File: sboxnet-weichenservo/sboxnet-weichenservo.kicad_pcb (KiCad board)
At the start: 2 copper layers, 35 parts, among them J1 Screw_Terminal_01x02, J10 Conn_01x03_Male, J11 Conn_01x03_Male, J12 Conn_01x03_Male, J2 Screw_Terminal_01x04, J3 Conn_02x17_Odd_Even, J4 Screw_Terminal_01x04, J5 Conn_01x03_Male, J6 Conn_01x03_Male, J7 Conn_01x03_Male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

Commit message: mit weichen-servo-ctrl
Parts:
- added BAR2: HDSP-4830_2 10x LED, Display:HDSP-4830, F.Cu at (-38.4, 102.3)
- added D3: BAT 54J NXP, Diode_SMD:D_SOD-323F, F.Cu at (-19.5, 146.1)
- added J13: Conn_02x08_Top_Bottom, Connector_PinSocket_2.54mm:PinSocket_2x10_P2.54mm_Vertical, F.Cu at (53.9, 170.0)
- added R2: 100, Resistor_SMD:R_1206_3216Metric_Pad1.42x1.75mm_HandSolder, F.Cu at (-30.5, 152.9)
- added RN1: 4816P-T02-471LF 15x470, Package_SO:SOIC-16W_5.3x10.2mm_P1.27mm, F.Cu at (-15.5, 138.7)
- added RN2: 4816P-2-103 13x 10k, Package_SO:SOIC-14W_7.5x9mm_P1.27mm, F.Cu at (-27.1, 138.0)
- added RN4: 4816P-T02-471LF 15x470, Package_SO:SOIC-16W_5.3x10.2mm_P1.27mm, F.Cu at (-23.7, 106.0)
- added SW5: SW_Push, sboxnet:JTP-1130, F.Cu at (-13.8, 103.8)
- added SW6: SW_Push, sboxnet:JTP-1130, F.Cu at (-24.0, 115.7)
- added SW7: SW_Push, sboxnet:JTP-1130, F.Cu at (-13.8, 111.3)
- added SW8: SW_Push, sboxnet:JTP-1130, F.Cu at (-4.34, 103.8)
- BAR1: value HDSP-4830_2 -> HDSP-4830_2 10x LED
- D1: moved to B.Cu
- RN3: value 8x 100 -> 4816P-1-101 8x 100
- U1: value MIC29302WU -> uA7805 D2PAK; footprint Package_TO_SOT_SMD:TO-263-5_TabPin3 -> Package_TO_SOT_SMD:ATPAK-2; moved to B.Cu
- moved U1 134.5 mm to (70.6, 188.7)
- moved D1 132.9 mm to (56.2, 189.5), turned to 180 degrees
- moved J6 114.7 mm to (70.2, 170.2), turned to 90 degrees
- moved J11 114.6 mm to (70.3, 145.3), turned to 90 degrees
- moved J8 107.5 mm to (70.1, 160.5), turned to 90 degrees
- moved J10 104.2 mm to (70.3, 149.9), turned to 90 degrees
- moved J9 98.2 mm to (70.2, 155.5), turned to 90 degrees
- moved J5 87.3 mm to (70.1, 174.8), turned to 90 degrees
- moved J7 87.3 mm to (70.0, 165.4), turned to 90 degrees
- moved J12 79.9 mm to (70.8, 141.0), turned to 90 degrees
- moved J4 56.6 mm to (133.8, 139.6)
- moved BAR1 49.4 mm to (58.0, 147.0), turned to 270 degrees
- moved J3 47.5 mm to (19.6, 193.2)
- moved J2 36.0 mm to (118.9, 141.6)
- moved J1 12.3 mm to (42.0, 189.5)
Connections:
- U1 pad 2: Net-(C1-Pad1) -> GND
- U1 pad 3: GND -> +5V
- U3 pad 16: VCC -> +5V
- U3 pad 5: Net-(R2-Pad1) -> Net-(D3-Pad1)

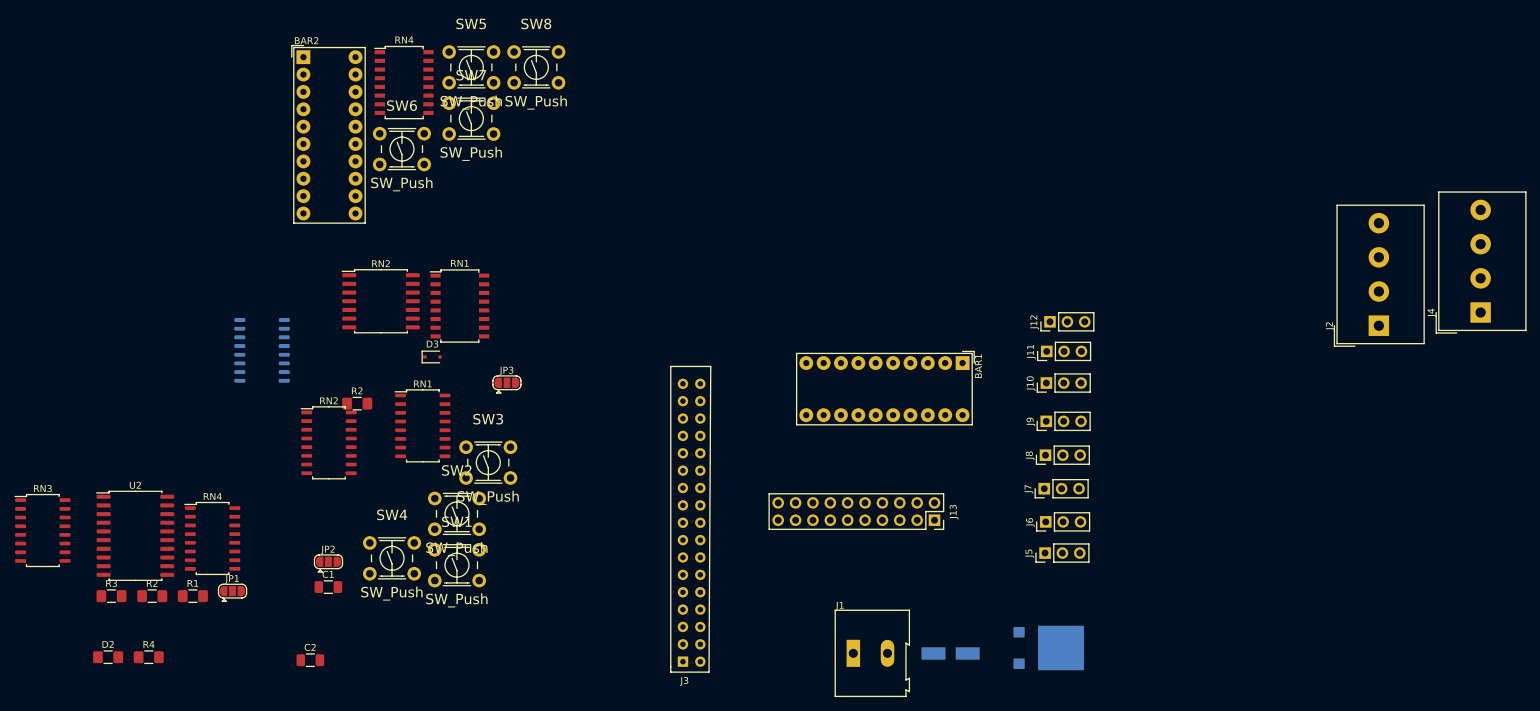
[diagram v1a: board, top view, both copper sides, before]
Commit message: weichenservo mit Modulkennung
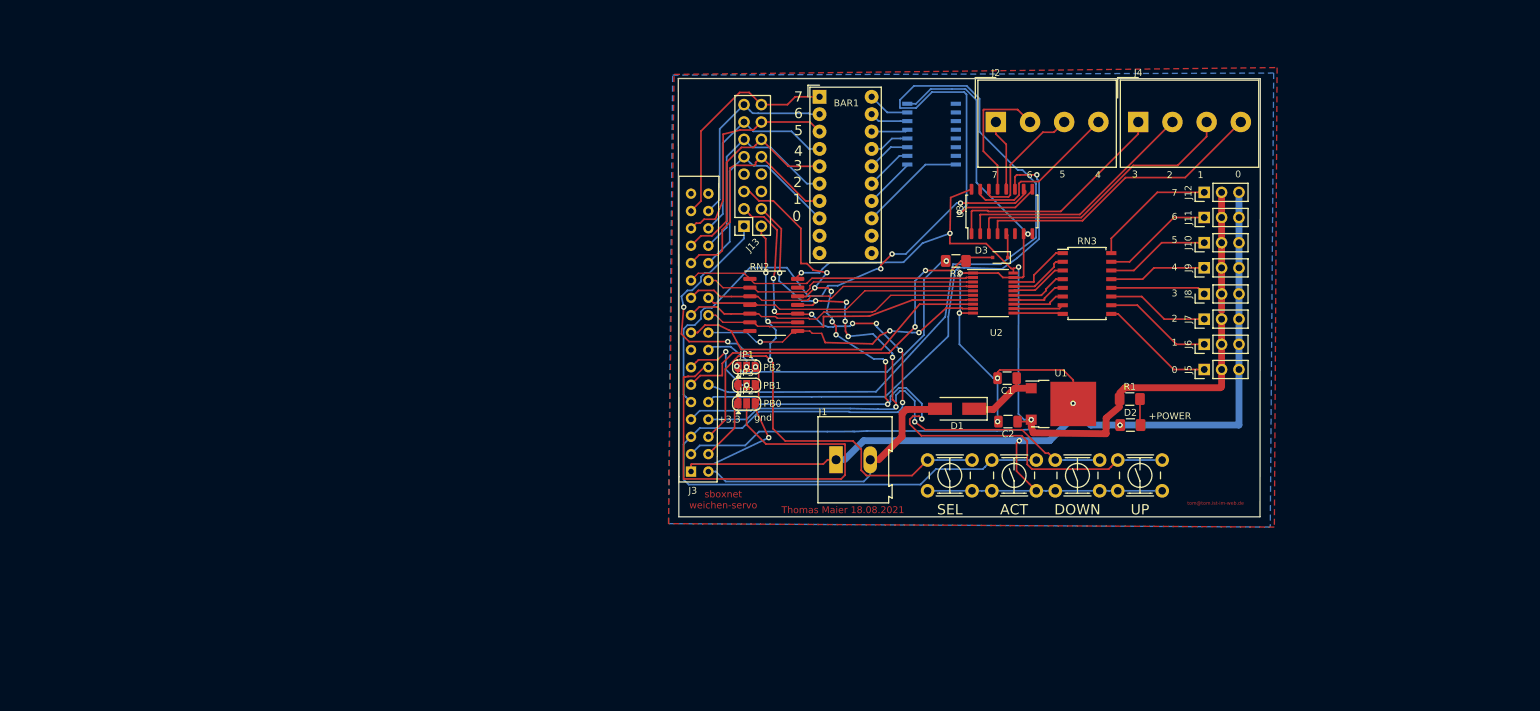
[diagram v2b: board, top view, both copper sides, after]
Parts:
- removed BAR2: HDSP-4830_2 10x LED, Display:HDSP-4830
- removed the R2 at (-30.5, 152.9)
- removed the R2 at (-60.5, 181.1)
- removed R3: 3k, Resistor_SMD:R_1206_3216Metric_Pad1.42x1.75mm_HandSolder
- removed R4: 10k, Resistor_SMD:R_1206_3216Metric_Pad1.42x1.75mm_HandSolder
- removed the RN1 at (-15.5, 138.7)
- removed the RN1 at (-20.9, 156.2)
- removed the RN2 at (-27.1, 138.0)
- removed the RN2 at (-34.7, 158.7)
- removed RN4: 4816P-T02-471LF 15x470, Package_SO:SOIC-16W_5.3x10.2mm_P1.27mm
- removed RN4: R_Network04 10k, Package_SO:SOIC-16_4.55x10.3mm_P1.27mm
- removed SW5, SW6, SW7, SW8: SW_Push, sboxnet:JTP-1130
- added R2: 100, Resistor_SMD:R_1206_3216Metric_Pad1.42x1.75mm_HandSolder, F.Cu at (57.0, 132.1)
- added RN1: 4816P-T02-471LF 15x470, Package_SO:SOIC-16W_5.3x10.2mm_P1.27mm, B.Cu at (53.5, 113.5)
- added RN2: 4816P-2-103 13x 10k, sboxnet:soic-14-8-6, F.Cu at (26.9, 133.4)
- D1, U1, U3: moved to F.Cu
- J13: footprint Connector_PinSocket_2.54mm:PinSocket_2x10_P2.54mm_Vertical -> Connector_PinSocket_2.54mm:PinSocket_2x08_P2.54mm_Vertical
- RN3: footprint Package_SO:SOIC-16_4.55x10.3mm_P1.27mm -> Package_SO:SOIC-16W_5.3x10.2mm_P1.27mm
- SW1: value SW_Push -> UP
- SW2: value SW_Push -> DOWN
- SW3: value SW_Push -> ACT
- SW4: value SW_Push -> SEL
- U2: footprint Package_SO:SOIC-20W_7.5x12.8mm_P1.27mm -> Package_SO:TSSOP-20_4.4x6.5mm_P0.65mm
- moved RN3 156.9 mm to (76.2, 135.4)
- moved D2 153.3 mm to (82.5, 156.1)
- moved R1 140.0 mm to (82.5, 152.3)
- moved U2 130.4 mm to (62.5, 136.8)
- moved U3 110.1 mm to (63.8, 124.8), turned to 90 degrees
- moved C2 107.8 mm to (64.6, 155.6), turned to 180 degrees
- moved C1 103.9 mm to (64.5, 149.2), turned to 180 degrees
- moved SW1 100.7 mm to (83.9, 163.4)
- moved SW2 90.9 mm to (74.8, 163.4)
- moved D3 84.3 mm to (63.5, 131.6), turned to 180 degrees
- moved SW4 82.5 mm to (56.1, 163.4)
- moved JP1 82.0 mm to (26.4, 147.6)
- moved SW3 76.9 mm to (65.5, 163.4)
- moved JP2 65.4 mm to (26.4, 152.9)
- moved J2 63.4 mm to (62.9, 111.8), turned to 0 degrees
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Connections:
- BAR1 pad 13: Net-(BAR1-Pad13) -> /L7
- BAR1 pad 14: Net-(BAR1-Pad14) -> /L6
- BAR1 pad 15: Net-(BAR1-Pad15) -> /L5
- BAR1 pad 16: Net-(BAR1-Pad16) -> /L4
- BAR1 pad 17: Net-(BAR1-Pad17) -> /L3
- BAR1 pad 18: Net-(BAR1-Pad18) -> /L2
- BAR1 pad 19: Net-(BAR1-Pad19) -> /L1
- BAR1 pad 20: Net-(BAR1-Pad20) -> /L0
- J13 pad 10: PD6 -> PD1
- J13 pad 11: PD5 -> PD2
- J13 pad 12: PD4 -> PD3
- J13 pad 13: PD3 -> PD4
- J13 pad 14: PD2 -> PD5
- J13 pad 15: PD1 -> PD6
- J13 pad 16: PD0 -> PD7
- J13 pad 9: PD7 -> PD0
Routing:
- net GND: track 0.00 -> 316.3 mm, vias 0 -> 12
- net +5V: track 0.00 -> 189.1 mm, vias 0 -> 4
- net PA1: track 0.00 -> 140.8 mm, vias 0 -> 7
- net PA6: track 0.00 -> 140.1 mm, vias 0 -> 1
- net PA3: track 0.00 -> 134.9 mm, vias 0 -> 8
- net PA2: track 0.00 -> 112.9 mm, vias 0 -> 8
- net PA0: track 0.00 -> 88.3 mm, vias 0 -> 3
- net PA4: track 0.00 -> 77.3 mm, vias 0 -> 1
- net PA5: track 0.00 -> 74.6 mm, vias 0 -> 3
- net PB0: track 0.00 -> 66.1 mm
- net +3V3: track 0.00 -> 57.0 mm, vias 0 -> 2
- net PA7: track 0.00 -> 56.8 mm, vias 0 -> 2
- net PC1: track 0.00 -> 49.3 mm
- net PC5: track 0.00 -> 44.8 mm
- net PC3: track 0.00 -> 43.9 mm
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- added copper zone on B.Cu, net GND
- added copper zone on F.Cu, net GND
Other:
- board outline added: 85.1 x 64.1 mm
- board text added: "+3.3"
- board text added: "+POWER"
- board text added: "0"
- board text added: "1"
- board text added: "2"
- board text added: "3"
- board text added: "4"
- board text added: "5"
- board text added: "6"
- board text added: "7"
- board text added: "PB0"
- board text added: "PB1"
- board text added: "PB2"
- board text added: "Thomas Maier 18.08.2021"
- board text added: "gnd"
- board text added: "sboxnet weichen-servo"
- board text added: "tom@tom.ist-im-web.de"

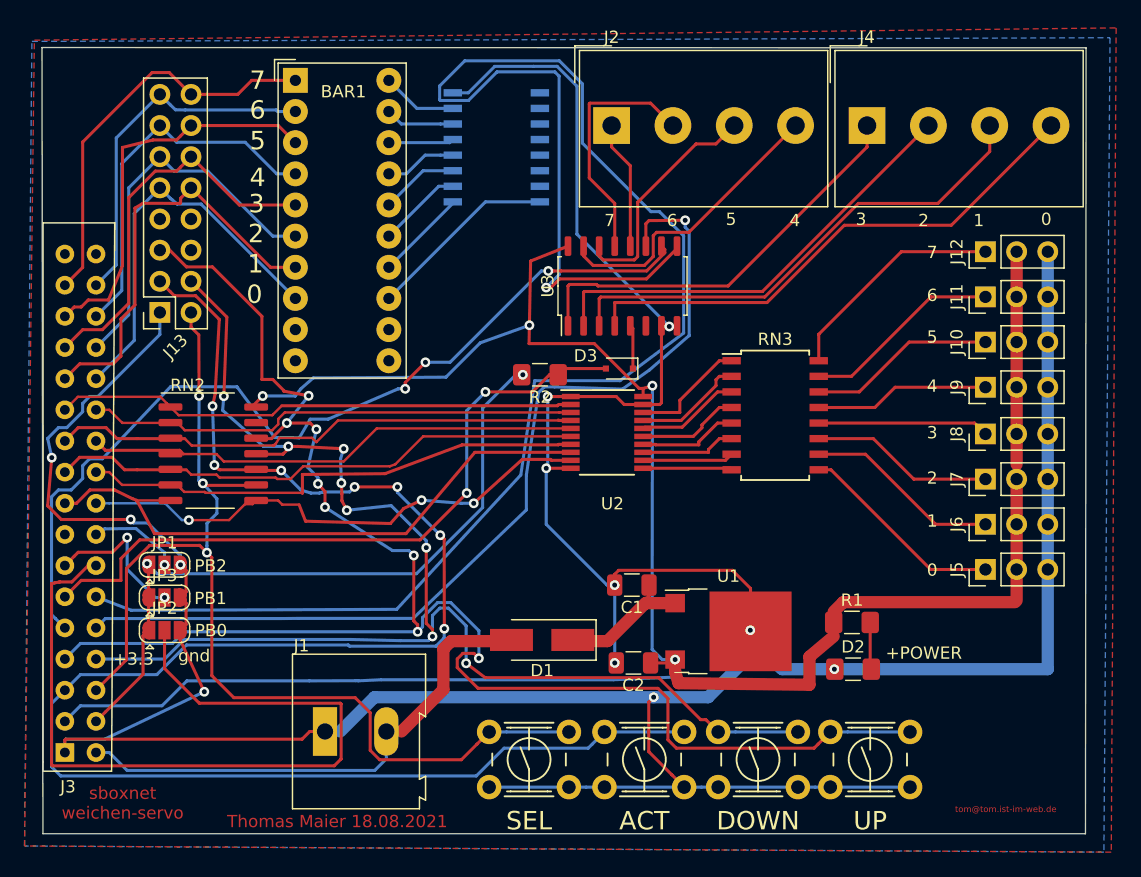
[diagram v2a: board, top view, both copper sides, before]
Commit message: weichen-servo mit Mounting Holes
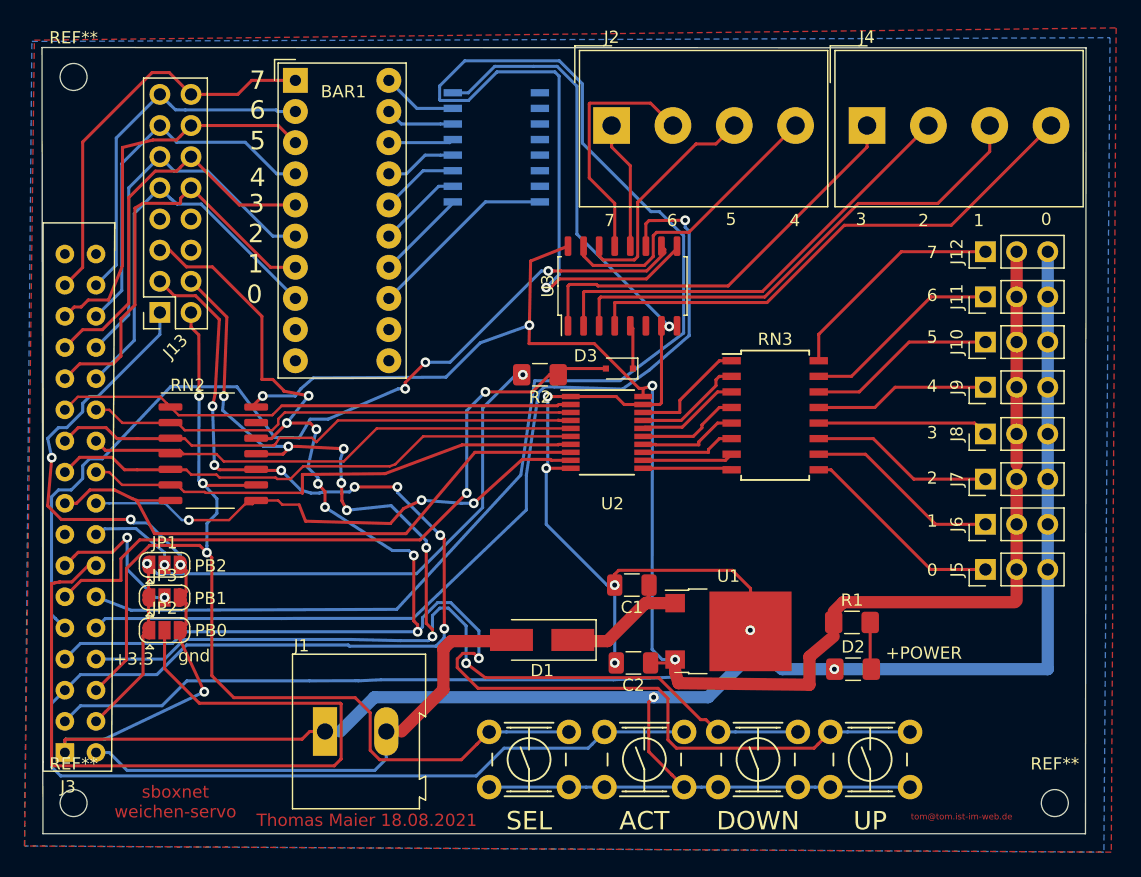
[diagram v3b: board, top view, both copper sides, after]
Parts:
- added REF**: MountingHole_2.2mm_M2, MountingHole:MountingHole_2.2mm_M2, F.Cu at (99.0, 167.0)
- added REF**: MountingHole_2.2mm_M2, MountingHole:MountingHole_2.2mm_M2, F.Cu at (19.0, 167.0)
- added REF**: MountingHole_2.2mm_M2, MountingHole:MountingHole_2.2mm_M2, F.Cu at (19.0, 107.8)
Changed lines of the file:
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@@
     (tracks 868)
     (zones 0)
-    (modules 34)
+    (modules 37)
     (nets 86)
   )
@@
     (add_net PD7)
   )
+  (module MountingHole:MountingHole_2.2mm_M2 (layer F.Cu)
+    (at 99 167)
+    (descr "Mounting Hole 2.2mm, no annular, M2")
+    (tags "mounting hole 2.2mm no annular m2")
+    (attr virtual)
+    (fp_text reference REF** (at 0 -3.2) (layer F.SilkS)
+      (effects (font (size 1 1) (thickness 0.15)))
+    )
+    (fp_text value MountingHole_2.2mm_M2 (at 0 3.2) (layer F.Fab) hide
+      (effects (font (size 1 1) (thickness 0.15)))
+    )
+    (fp_circle (center 0 0) (end 2.45 0) (layer F.CrtYd) (width 0.05))
+    (fp_circle (center 0 0) (end 2.2 0) (layer Cmts.User) (width 0.15))
+    (fp_text user %R (at 0.3 0) (layer F.Fab)
+      (effects (font (size 1 1) (thickness 0.15)))
+    )
+    (pad 1 np_thru_hole circle (at 0 0) (size 2.2 2.2) (drill 2.2) (layers *.Cu *.Mask))
+  )
+  (module MountingHole:MountingHole_2.2mm_M2 (layer F.Cu)
+    (at 19 167)
+    (descr "Mounting Hole 2.2mm, no annular, M2")
+    (tags "mounting hole 2.2mm no annular m2")
+    (attr virtual)
+    (fp_text reference REF** (at 0 -3.2) (layer F.SilkS)
+      (effects (font (size 1 1) (thickness 0.15)))
+    )
+    (fp_text value MountingHole_2.2mm_M2 (at 0 3.2) (layer F.Fab) hide
+      (effects (font (size 1 1) (thickness 0.15)))
+    )
+    (fp_circle (center 0 0) (end 2.45 0) (layer F.CrtYd) (width 0.05))
+    (fp_circle (center 0 0) (end 2.2 0) (layer Cmts.User) (width 0.15))
+    (fp_text user %R (at 0.3 0) (layer F.Fab)
+      (effects (font (size 1 1) (thickness 0.15)))
+    )
+    (pad 1 np_thru_hole circle (at 0 0) (size 2.2 2.2) (drill 2.2) (layers *.Cu *.Mask))
+  )
+  (module MountingHole:MountingHole_2.2mm_M2 (layer F.Cu)
+    (at 19 107.8)
+    (descr "Mounting Hole 2.2mm, no annular, M2")
+    (tags "mounting hole 2.2mm no annular m2")
+    (attr virtual)
+    (fp_text reference REF** (at 0 -3.2) (layer F.SilkS)
+      (effects (font (size 1 1) (thickness 0.15)))
+    )
+    (fp_text value MountingHole_2.2mm_M2 (at 0 3.2) (layer F.Fab) hide
+      (effects (font (size 1 1) (thickness 0.15)))
+    )
+    (fp_circle (center 0 0) (end 2.45 0) (layer F.CrtYd) (width 0.05))
+    (fp_circle (center 0 0) (end 2.2 0) (layer Cmts.User) (width 0.15))
+    (fp_text user %R (at 0.3 0) (layer F.Fab)
+      (effects (font (size 1 1) (thickness 0.15)))
+    )
+    (pad 1 np_thru_hole circle (at 0 0) (size 2.2 2.2) (drill 2.2) (layers *.Cu *.Mask))
+  )
   (module sboxnet:soic-14-8-6 (layer F.Cu)
     (at 26.8986 133.4389)
@@
     (effects (font (size 1 1) (thickness 0.15)))
   )
-  (gr_text tom@tom.ist-im-web.de (at 95 167.5) (layer F.Cu)
+  (gr_text tom@tom.ist-im-web.de (at 91.4 168.1) (layer F.Cu)
     (effects (font (size 0.5 0.5) (thickness 0.1)))
   )
-  (gr_text "Thomas Maier 18.08.2021" (at 40.5 168.5) (layer F.Cu)
+  (gr_text "Thomas Maier 18.08.2021" (at 42.9 168.4) (layer F.Cu)
     (effects (font (size 1 1) (thickness 0.15)))
   )
-  (gr_text "sboxnet\nweichen-servo" (at 23 167) (layer F.Cu)
+  (gr_text "sboxnet\nweichen-servo" (at 27.3 166.9) (layer F.Cu)
     (effects (font (size 1 1) (thickness 0.15)))
   )
